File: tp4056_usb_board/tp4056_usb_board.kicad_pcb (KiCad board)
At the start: 2 copper layers, 26 x 17.2 mm, 22 parts, among them J1 USB_OTG, J2 TP4056, J3 DW01, J4 8205A, J5 TEST_2P, U1 TP4056_BREAKOUT, U2 CP2102N-20P

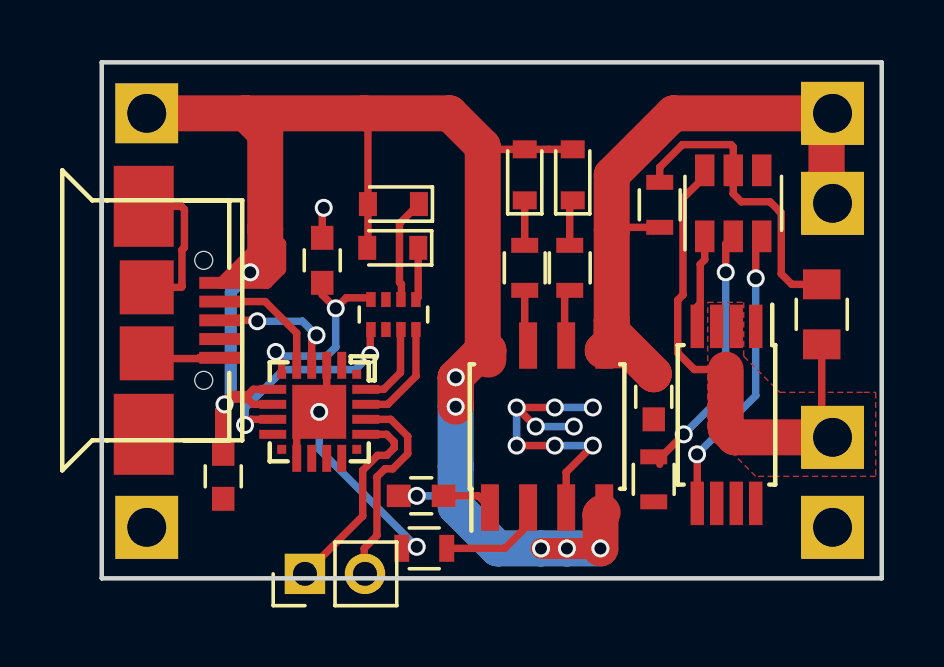
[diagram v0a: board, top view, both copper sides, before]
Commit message: Renaming the TP4056 board files + small fixups
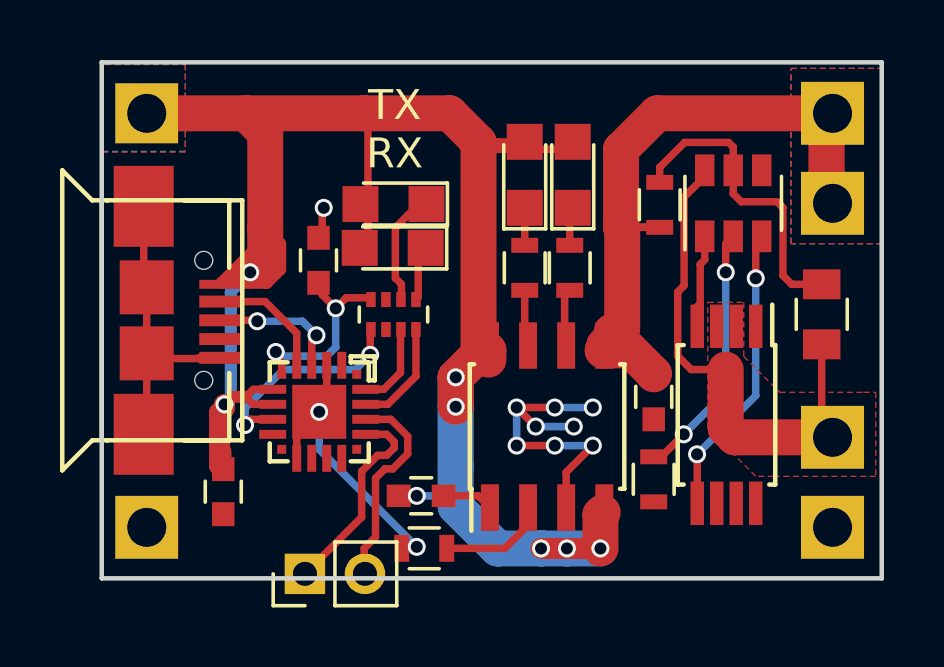
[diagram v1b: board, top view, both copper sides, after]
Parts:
- D1, D2, D3, D4: footprint Diodes_SMD:D_0603 -> LEDs:LED_0805
- moved C4 0.51 mm to (128.7, 131.7)
- moved C5 0.12 mm to (131.8, 124.0)
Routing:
- net VSS: track 26.0 -> 34.3 mm
- net +5V: track 69.4 -> 74.9 mm
- net GND: track 29.6 -> 32.1 mm
- added copper zone on B.Cu, net +5V
- added copper zone on F.Cu, net +5V
- added copper zone on B.Cu, net VSS
- added copper zone on F.Cu, net VSS
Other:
- board text added: "TX RX"

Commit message: Fixing the schematic - adding a jumper (instead of the capacitor) to the TEMP pin
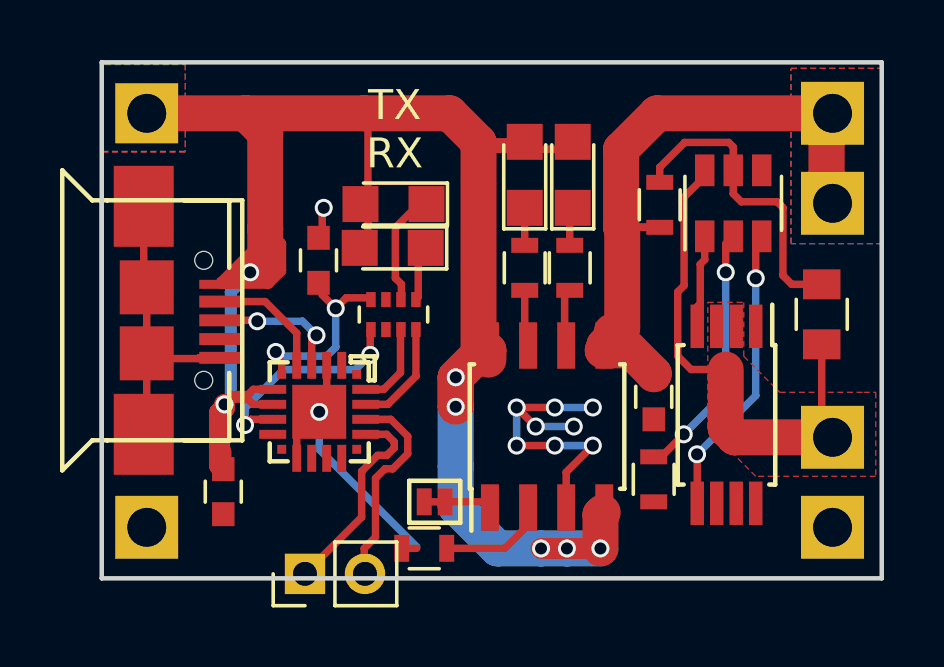
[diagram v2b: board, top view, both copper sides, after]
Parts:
- removed C1: C, Capacitors_SMD:C_0603
- added JP1: TEMP, footprints:GS2_SMALL, F.Cu at (136.1, 132.1)
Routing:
- net +5V: track 74.9 -> 73.4 mm, vias 8 -> 7
- net GND: track 32.1 -> 32.9 mm, vias 11 -> 10

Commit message: TP4056 board - changing current set resistor FP to 1206 (better change to 0805 in the next rev?)
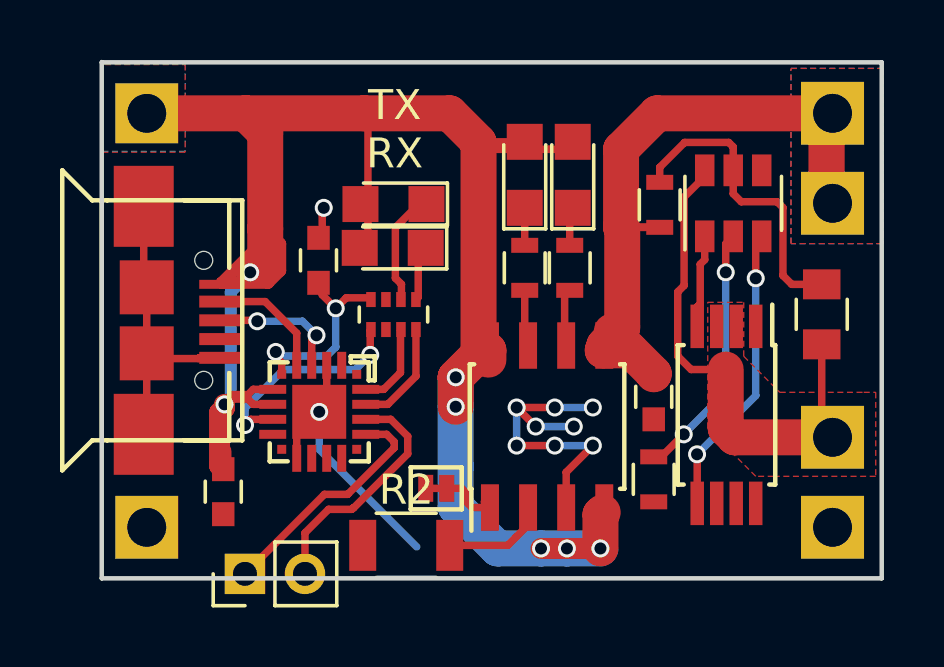
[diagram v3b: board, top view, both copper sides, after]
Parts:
- R2: footprint Resistors_SMD:R_0603 -> Resistors_SMD:R_1206
- moved J5 2.00 mm to (129.4, 134.4)
- moved R2 0.61 mm to (134.8, 133.5)
- moved JP1 0.45 mm to (136.1, 131.6)
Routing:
- net RXD: track 6.86 -> 7.97 mm
- net TXD: track 7.12 -> 8.10 mm
- net GND: track 32.9 -> 32.3 mm
- net Net-(J2-Pad1): track 1.90 -> 2.49 mm
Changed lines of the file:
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@@
   (general
     (links 58)
-    (no_connects 1)
+    (no_connects 0)
     (area 122.625 115.373 151.175 137.697619)
     (thickness 1.6)
     (drawings 13)
-    (tracks 267)
+    (tracks 268)
     (zones 0)
     (modules 22)
@@
     (add_net VSS)
   )
+  (module Resistors_SMD:R_1206 (layer F.Cu)
+    (at 134.75 133.5)
+    (descr "Resistor SMD 1206, reflow soldering, Vishay (see dcrcw.pdf)")
+    (tags "resistor 1206")
+    (attr smd)
+    (fp_text reference R2 (at 0 -1.85) (layer F.SilkS)
+      (effects (font (size 1 1) (thickness 0.15)))
+    )
+    (fp_text value R (at 0 1.95) (layer F.Fab)
+      (effects (font (size 1 1) (thickness 0.15)))
+    )
+    (fp_text user %R (at 0 0) (layer F.Fab)
+      (effects (font (size 0.7 0.7) (thickness 0.105)))
+    )
+    (fp_line (start -1.6 0.8) (end -1.6 -0.8) (layer F.Fab) (width 0.1))
+    (fp_line (start 1.6 0.8) (end -1.6 0.8) (layer F.Fab) (width 0.1))
+    (fp_line (start 1.6 -0.8) (end 1.6 0.8) (layer F.Fab) (width 0.1))
+    (fp_line (start -1.6 -0.8) (end 1.6 -0.8) (layer F.Fab) (width 0.1))
+    (fp_line (start 1 1.07) (end -1 1.07) (layer F.SilkS) (width 0.12))
+    (fp_line (start -1 -1.07) (end 1 -1.07) (layer F.SilkS) (width 0.12))
+    (fp_line (start -2.15 -1.11) (end 2.15 -1.11) (layer F.CrtYd) (width 0.05))
+    (fp_line (start -2.15 -1.11) (end -2.15 1.1) (layer F.CrtYd) (width 0.05))
+    (fp_line (start 2.15 1.1) (end 2.15 -1.11) (layer F.CrtYd) (width 0.05))
+    (fp_line (start 2.15 1.1) (end -2.15 1.1) (layer F.CrtYd) (width 0.05))
+    (pad 1 smd rect (at -1.45 0) (size 0.9 1.7) (layers F.Cu F.Paste F.Mask)
+      (net 3 GND))
+    (pad 2 smd rect (at 1.45 0) (size 0.9 1.7) (layers F.Cu F.Paste F.Mask)
+      (net 8 "Net-(J2-Pad2)"))
+    (model ${KISYS3DMOD}/Resistors_SMD.3dshapes/R_1206.wrl
+      (at (xyz 0 0 0))
+      (scale (xyz 1 1 1))
+      (rotate (xyz 0 0 0))
+    )
+  )
   (module Pin_Headers:Pin_Header_Straight_1x02_Pitch2.00mm (layer F.Cu)
-    (at 131.375 134.45 90)
+    (at 129.375 134.45 90)
     (descr "Through hole straight pin header, 1x02, 2.00mm pitch, single row")
     (tags "Through hole pin header THT 1x02 2.00mm single row")
@@
   )
   (module Resistors_SMD:R_0603 (layer F.Cu)
-    (at 135.35 133.6)
-    (descr "Resistor SMD 0603, reflow soldering, Vishay (see dcrcw.pdf)")
-    (tags "resistor 0603")
-    (attr smd)
-    (fp_text reference R2 (at 0 -1.45) (layer F.SilkS) hide
-      (effects (font (size 1 1) (thickness 0.15)))
-    )
-    (fp_text value R (at 0 1.5) (layer F.Fab)
-      (effects (font (size 1 1) (thickness 0.15)))
-    )
-    (fp_text user %R (at 0 0) (layer F.Fab)
-      (effects (font (size 0.4 0.4) (thickness 0.075)))
-    )
-    (fp_line (start -0.8 0.4) (end -0.8 -0.4) (layer F.Fab) (width 0.1))
-    (fp_line (start 0.8 0.4) (end -0.8 0.4) (layer F.Fab) (width 0.1))
-    (fp_line (start 0.8 -0.4) (end 0.8 0.4) (layer F.Fab) (width 0.1))
-    (fp_line (start -0.8 -0.4) (end 0.8 -0.4) (layer F.Fab) (width 0.1))
-    (fp_line (start 0.5 0.68) (end -0.5 0.68) (layer F.SilkS) (width 0.12))
-    (fp_line (start -0.5 -0.68) (end 0.5 -0.68) (layer F.SilkS) (width 0.12))
-    (fp_line (start -1.25 -0.7) (end 1.25 -0.7) (layer F.CrtYd) (width 0.05))
-    (fp_line (start -1.25 -0.7) (end -1.25 0.7) (layer F.CrtYd) (width 0.05))
-    (fp_line (start 1.25 0.7) (end 1.25 -0.7) (layer F.CrtYd) (width 0.05))
-    (fp_line (start 1.25 0.7) (end -1.25 0.7) (layer F.CrtYd) (width 0.05))
-    (pad 1 smd rect (at -0.75 0) (size 0.5 0.9) (layers F.Cu F.Paste F.Mask)
-      (net 3 GND))
-    (pad 2 smd rect (at 0.75 0) (size 0.5 0.9) (layers F.Cu F.Paste F.Mask)
-      (net 8 "Net-(J2-Pad2)"))
-    (model ${KISYS3DMOD}/Resistors_SMD.3dshapes/R_0603.wrl
-      (at (xyz 0 0 0))
-      (scale (xyz 1 1 1))
-      (rotate (xyz 0 0 0))
-    )
-  )
-  (module Resistors_SMD:R_0603 (layer F.Cu)
     (at 140.2 124.25 270)
     (descr "Resistor SMD 0603, reflow soldering, Vishay (see dcrcw.pdf)")
@@
   )
   (module footprints:GS2_SMALL (layer F.Cu)
-    (at 136.05 132.05 90)
+    (at 136.1 131.6 90)
     (descr "3-pin solder bridge")
     (tags "solder bridge")
@@
   (segment (start 141.7 122.9) (end 141.6 123) (width 0.25) (layer F.Cu) (net 2))
   (segment (start 141.6 126.7) (end 141.3 127) (width 1.2) (layer F.Cu) (net 2))
-  (segment (start 134.6 133.6) (end 135.1 133.6) (width 0.25) (layer F.Cu) (net 3))
+  (segment (start 135.4 131.6) (end 136.1 131.6) (width 0.25) (layer F.Cu) (net 3))
   (segment (start 126 122.2) (end 126 124.8) (width 0.25) (layer F.Cu) (net 3))
   (segment (start 126 124.8) (end 126.1 124.9) (width 0.25) (layer F.Cu) (net 3))
@@
   (segment (start 140.081 131.064) (end 140.97 130.175) (width 0.25) (layer F.Cu) (net 3))
   (via (at 140.97 130.175) (size 0.6) (drill 0.4) (layers F.Cu B.Cu) (net 3))
-  (segment (start 136.05 132.05) (end 135.3 132.05) (width 0.25) (layer F.Cu) (net 3))
-  (segment (start 135.3 132.05) (end 135.35 132.05) (width 0.25) (layer F.Cu) (net 3))
   (segment (start 143.2 121.4) (end 143.2 120.9) (width 0.25) (layer F.Cu) (net 4))
   (segment (start 143.2 120.9) (end 144.029635 120.070365) (width 0.25) (layer F.Cu) (net 4))
@@
   (segment (start 140.2 123.5) (end 140.2 122.1) (width 0.25) (layer F.Cu) (net 7))
   (segment (start 140.2 122.1) (end 140.3 122) (width 0.25) (layer F.Cu) (net 7))
-  (segment (start 136.1 133.6) (end 138.035 133.6) (width 0.25) (layer F.Cu) (net 8))
-  (segment (start 138.035 133.6) (end 138.76 132.875) (width 0.25) (layer F.Cu) (net 8))
+  (segment (start 138.4 133.235) (end 138.76 132.875) (width 0.25) (layer F.Cu) (net 8))
+  (segment (start 136.2 133.5) (end 138.135 133.5) (width 0.25) (layer F.Cu) (net 8))
+  (segment (start 138.135 133.5) (end 138.4 133.235) (width 0.25) (layer F.Cu) (net 8))
   (segment (start 138.76 132.875) (end 138.76 132.4) (width 0.25) (layer F.Cu) (net 8))
   (segment (start 140.03 127) (end 140.03 125.17) (width 0.25) (layer F.Cu) (net 9))
@@
   (segment (start 134.559001 126.321999) (end 134.574 126.307) (width 0.25) (layer F.Cu) (net 21))
   (segment (start 133.4 128.3) (end 134 128.3) (width 0.25) (layer F.Cu) (net 21))
-  (segment (start 131.375 134.45) (end 133.264025 132.560975) (width 0.25) (layer F.Cu) (net 22))
-  (segment (start 133.264025 132.560975) (end 133.264025 131.035975) (width 0.25) (layer F.Cu) (net 22))
-  (segment (start 133.264025 131.035975) (end 133.80001 130.49999) (width 0.25) (layer F.Cu) (net 22))
-  (segment (start 133.80001 130.49999) (end 134.10001 130.49999) (width 0.25) (layer F.Cu) (net 22))
-  (segment (start 134.10001 130.49999) (end 134.34999 130.25001) (width 0.25) (layer F.Cu) (net 22))
   (segment (start 134.34999 130.25001) (end 134.34999 130.051398) (width 0.25) (layer F.Cu) (net 22))
+  (segment (start 134.098592 129.8) (end 133.4 129.8) (width 0.25) (layer F.Cu) (net 22))
+  (segment (start 129.375 134.45) (end 132.025 131.8) (width 0.25) (layer F.Cu) (net 22))
+  (segment (start 132.025 131.8) (end 132.8 131.8) (width 0.25) (layer F.Cu) (net 22))
+  (segment (start 132.8 131.8) (end 134.34999 130.25001) (width 0.25) (layer F.Cu) (net 22))
   (segment (start 134.34999 130.051398) (end 134.098592 129.8) (width 0.25) (layer F.Cu) (net 22))
-  (segment (start 134.098592 129.8) (end 133.4 129.8) (width 0.25) (layer F.Cu) (net 22))
+  (segment (start 132.16141 132.3) (end 131.375 133.08641) (width 0.25) (layer F.Cu) (net 23))
+  (segment (start 131.375 133.08641) (end 131.375 134.45) (width 0.25) (layer F.Cu) (net 23))
+  (segment (start 134.8 130.45) (end 133 132.25) (width 0.25) (layer F.Cu) (net 23))
+  (segment (start 133 132.25) (end 132.98641 132.25) (width 0.25) (layer F.Cu) (net 23))
+  (segment (start 132.98641 132.25) (end 132.93641 132.3) (width 0.25) (layer F.Cu) (net 23))
+  (segment (start 132.93641 132.3) (end 132.16141 132.3) (width 0.25) (layer F.Cu) (net 23))
+  (segment (start 134.800001 129.864998) (end 134.8 130.45) (width 0.25) (layer F.Cu) (net 23))
+  (segment (start 134.235002 129.3) (end 134.800001 129.864998) (width 0.25) (layer F.Cu) (net 23))
   (segment (start 133.4 129.3) (end 134.235002 129.3) (width 0.25) (layer F.Cu) (net 23))
-  (segment (start 134.235002 129.3) (end 134.8 129.864998) (width 0.25) (layer F.Cu) (net 23))
-  (segment (start 133.35 133.6) (end 133.35 134.6) (width 0.25) (layer F.Cu) (net 23))
-  (segment (start 134.8 129.864998) (end 134.8 130.45) (width 0.25) (layer F.Cu) (net 23))
-  (segment (start 134.8 130.45) (end 134.3 130.95) (width 0.25) (layer F.Cu) (net 23))
-  (segment (start 134.3 130.95) (end 134.039998 130.95) (width 0.25) (layer F.Cu) (net 23))
-  (segment (start 134.039998 130.95) (end 133.726049 131.263949) (width 0.25) (layer F.Cu) (net 23))
-  (segment (start 133.726049 131.263949) (end 133.726049 133.223951) (width 0.25) (layer F.Cu) (net 23))
-  (segment (start 133.726049 133.223951) (end 133.35 133.6) (width 0.25) (layer F.Cu) (net 23))
-  (segment (start 136.05 132.05) (end 137.351 132.05) (width 0.25) (layer F.Cu) (net 24))
+  (segment (start 136.8 132.1) (end 136.94 132.24) (width 0.25) (layer F.Cu) (net 24))
+  (segment (start 136.6 131.6) (end 136.8 131.8) (width 0.25) (layer F.Cu) (net 24))
+  (segment (start 136.8 131.8) (end 136.8 132.1) (width 0.25) (layer F.Cu) (net 24))
+  (segment (start 136.1 131.6) (end 136.6 131.6) (width 0.25) (layer F.Cu) (net 24))
+  (segment (start 136.94 132.24) (end 137.541 132.24) (width 0.25) (layer F.Cu) (net 24))
   (segment (start 137.351 132.05) (end 137.541 132.24) (width 0.25) (layer F.Cu) (net 24))
   (segment (start 137.49 132.065) (end 137.49 132.4) (width 0.25) (layer F.Cu) (net 24))
